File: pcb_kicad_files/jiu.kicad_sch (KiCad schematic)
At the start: 175 parts, among them J1 2x3 2.54mm pitch pin header, J2 TYPE-C-31-M-12, J3 1x5 2.54mm pitch pin header, J4 2x9 2.54mm pitch pin header, J5 RESET PINS, Q1 2N7002, SW1 1U, SW10 1U, SW11 1U, SW12 1U, SW13 1U, SW14 1U, SW15 1U, SW16 2u, SW17 1.5U, SW18 1U, SW19 1U, SW2 1U, SW20 1U, SW21 1U, SW22 1U, SW23 1U, SW24 1U, SW25 1U, SW26 1U, SW27 1U, SW28 1U, SW29 1U, SW3 1U, SW30 1.5U, SW31 1U, SW32 1.75U, SW33 1U, SW34 1U, SW35 1U, SW36 1U, SW37 1U, SW38 1U, SW39 1U, SW4 1U, SW40 1U, SW41 1U, SW42 1U, SW43 1U, SW44 2.25U, SW45 1U, SW46 1.25U, SW47 2.25U, SW48 1U, SW49 1U, SW5 1U, SW50 1U, SW51 1U, SW52 1U, SW53 1U, SW54 1U, SW55 1U, SW56 1U, SW57 1U, SW58 1.75U, SW59 1U, SW6 1U, SW60 1U, SW61 1.5U, SW62 1U, SW63 1.5U, SW64 7U, SW65 1.5U, SW66 1U, SW67 1U, SW68 1U, SW69 1.25U, SW7 1U, SW70 1.25U, SW71 1.25U, SW72 6.25U, SW73 1.25U, SW8 1U, SW9 1U, U1 SRV05-4-P-T7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

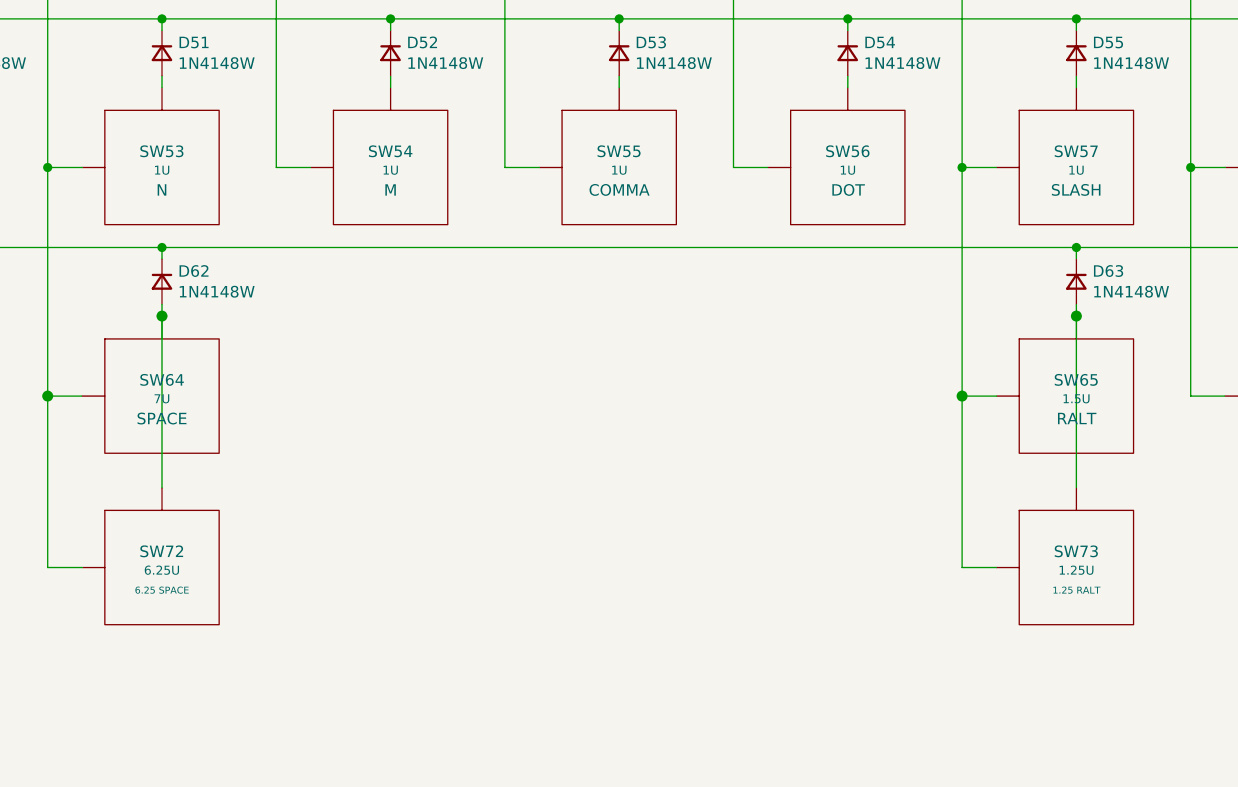
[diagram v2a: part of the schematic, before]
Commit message: Fix missing 6.25U bottom row key
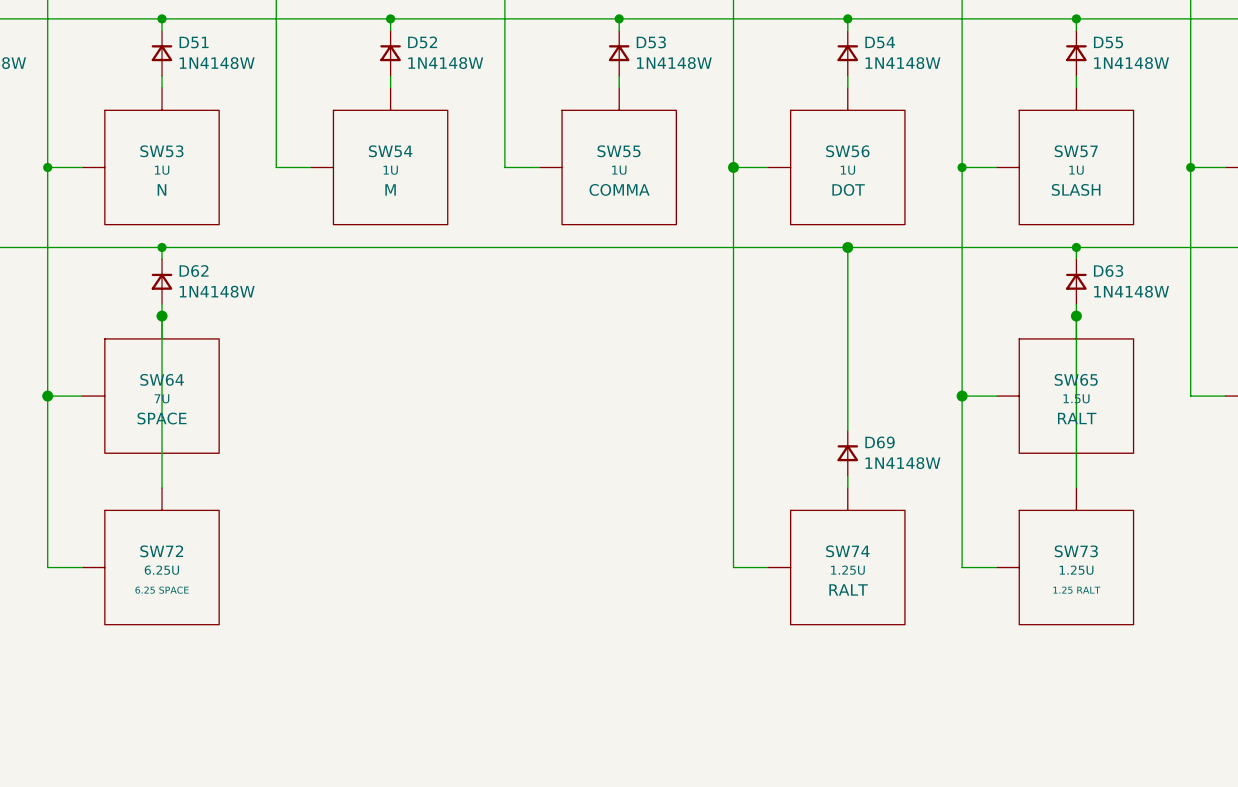
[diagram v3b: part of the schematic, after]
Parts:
- added D69: 1N4148W, acheron_Components:D_SOD-123, symbol Device:D_Small
- added SW74: 1.25U, acheron_MX_SolderMask:MX125, symbol acheronSymbols:MXSwitch
- D68: Manufacturer Shikues -> (none)
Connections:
- net C9: now also SW74.1 (Col)
- net R4: now also D69.1 (K)
- new net: D69.2 (A), SW74.2 (Row)
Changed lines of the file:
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@@
   (title_block
     (title "Jiu schematic")
-    (date "2021-02-21")
-    (rev "v1.1.8")
+    (date "2021-03-08")
+    (rev "v1.1.9")
     (company "Designed by Gondolindrim")
   )
@@
   (junction (at 266.7 76.2) (diameter 1.016) (color 0 0 0 0))
   (junction (at 266.7 101.6) (diameter 1.016) (color 0 0 0 0))
+  (junction (at 266.7 127) (diameter 1.2192) (color 0 0 0 0))
   (junction (at 271.145 332.105) (diameter 1.016) (color 0 0 0 0))
   (junction (at 271.145 338.455) (diameter 1.016) (color 0 0 0 0))
@@
   (junction (at 279.4 85.09) (diameter 1.016) (color 0 0 0 0))
   (junction (at 279.4 110.49) (diameter 1.016) (color 0 0 0 0))
+  (junction (at 279.4 135.89) (diameter 1.2192) (color 0 0 0 0))
   (junction (at 282.575 277.495) (diameter 1.016) (color 0 0 0 0))
   (junction (at 288.925 277.495) (diameter 1.016) (color 0 0 0 0))
@@
     (stroke (width 0) (type solid) (color 0 0 0 0))
   )
-  (wire (pts (xy 203.2 135.89) (xy 304.8 135.89))
+  (wire (pts (xy 203.2 135.89) (xy 279.4 135.89))
     (stroke (width 0) (type solid) (color 0 0 0 0))
   )
@@
     (stroke (width 0) (type solid) (color 0 0 0 0))
   )
+  (wire (pts (xy 266.7 127) (xy 266.7 171.45))
+    (stroke (width 0) (type solid) (color 0 0 0 0))
+  )
   (wire (pts (xy 270.51 76.2) (xy 266.7 76.2))
     (stroke (width 0) (type solid) (color 0 0 0 0))
@@
     (stroke (width 0) (type solid) (color 0 0 0 0))
   )
+  (wire (pts (xy 270.51 171.45) (xy 266.7 171.45))
+    (stroke (width 0) (type solid) (color 0 0 0 0))
+  )
   (wire (pts (xy 271.145 287.655) (xy 272.415 287.655))
     (stroke (width 0) (type solid) (color 0 0 0 0))
@@
     (stroke (width 0) (type solid) (color 0 0 0 0))
   )
+  (wire (pts (xy 279.4 135.89) (xy 279.4 156.21))
+    (stroke (width 0) (type solid) (color 0 0 0 0))
+  )
+  (wire (pts (xy 279.4 135.89) (xy 304.8 135.89))
+    (stroke (width 0) (type solid) (color 0 0 0 0))
+  )
+  (wire (pts (xy 279.4 161.29) (xy 279.4 162.56))
+    (stroke (width 0) (type solid) (color 0 0 0 0))
+  )
   (wire (pts (xy 282.575 273.05) (xy 282.575 277.495))
     (stroke (width 0) (type solid) (color 0 0 0 0))
@@
     (pin "2")
   )
+  (symbol (lib_id "Device:D_Small") (at 279.4 158.75 270) (unit 1)
+    (in_bom yes) (on_board yes)
+    (property "Reference" "D69" (id 0) (at 281.1781 157.6006 90)
+      (effects (font (size 1.27 1.27)) (justify left))
+    )
+    (property "Value" "1N4148W" (id 1) (at 281.1781 159.8993 90)
+      (effects (font (size 1.27 1.27)) (justify left))
+    )
+    (property "Footprint" "acheron_Components:D_SOD-123" (id 2) (at 279.4 158.75 90)
+      (effects (font (size 1.27 1.27)) hide)
+    )
+    (property "Datasheet" "~" (id 3) (at 279.4 158.75 90)
+      (effects (font (size 1.27 1.27)) hide)
+    )
+    (property "Package" "SOD-123" (id 4) (at 279.4 158.75 90)
+      (effects (font (size 1.27 1.27)) hide)
+    )
+    (pin "1")
+    (pin "2")
+  )
   (symbol (lib_id "Device:D_Small") (at 304.8 38.1 270) (unit 1)
     (in_bom yes) (on_board yes)
@@
       (effects (font (size 1.27 1.27)) hide)
     )
-    (property "Manufacturer" "Shikues" (id 4) (at 204.47 322.58 0)
-      (effects (font (size 1.27 1.27)) hide)
-    )
-    (property "LCSC Part Number" "C115330" (id 5) (at 204.47 322.58 0)
+    (property "LCSC Part Number" "C115330" (id 4) (at 204.47 322.58 0)
       (effects (font (size 1.27 1.27)) hide)
     )
@@
     (pin "2")
   )
+  (symbol (lib_id "acheronSymbols:MXSwitch") (at 279.4 171.45 0) (unit 1)
+    (in_bom no) (on_board yes)
+    (property "Reference" "SW74" (id 0) (at 279.4 169.6974 0))
+    (property "Value" "1.25U" (id 1) (at 279.4 171.7802 0)
+      (effects (font (size 0.9906 0.9906)))
+    )
+    (property "Footprint" "acheron_MX_SolderMask:MX125" (id 2) (at 279.4 171.45 0)
+      (effects (font (size 1.27 1.27)) hide)
+    )
+    (property "Datasheet" "" (id 3) (at 279.4 171.45 0)
+      (effects (font (size 1.27 1.27)) hide)
+    )
+    (property "Default keycode" "RALT" (id 4) (at 279.4 173.99 0))
+    (pin "1")
+    (pin "2")
+  )
   (symbol (lib_id "acheronSymbols:MXSwitch") (at 304.8 50.8 0) (unit 1)
     (in_bom no) (on_board yes)
@@
       (reference "D68") (unit 1) (value "RB060M-60") (footprint "acheron_Components:D_SOD-123")
     )
+    (path "/b11a079a-7715-44e5-8f45-742bb8e4c761"
+      (reference "D69") (unit 1) (value "1N4148W") (footprint "acheron_Components:D_SOD-123")
+    )
     (path "/0d47d058-12d7-4b9d-a82b-832091c19ada"
       (reference "F1") (unit 1) (value "mSMD110-16V") (footprint "acheron_Components:Fuse_1812_4532")
@@
       (reference "SW73") (unit 1) (value "1.25U") (footprint "acheron_MX_SolderMask:MX125")
     )
+    (path "/284362d5-314f-4ba3-9c4c-6f51d6510560"
+      (reference "SW74") (unit 1) (value "1.25U") (footprint "acheron_MX_SolderMask:MX125")
+    )
     (path "/c6a77dd8-927c-49d7-af6c-78d05d2184a0"

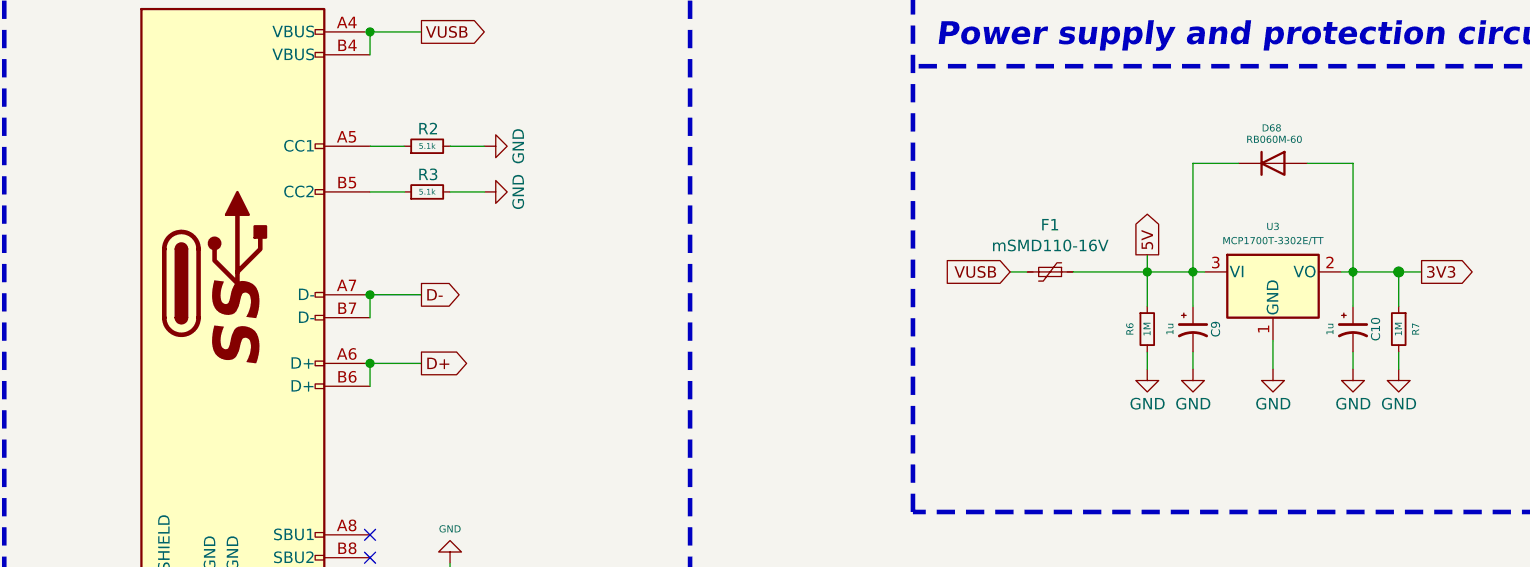
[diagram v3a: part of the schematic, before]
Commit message: gitignore, stab orientation
- Added backup files to gitignore
- Fix enter, right shift keys stab orientations
- New KiCAD version
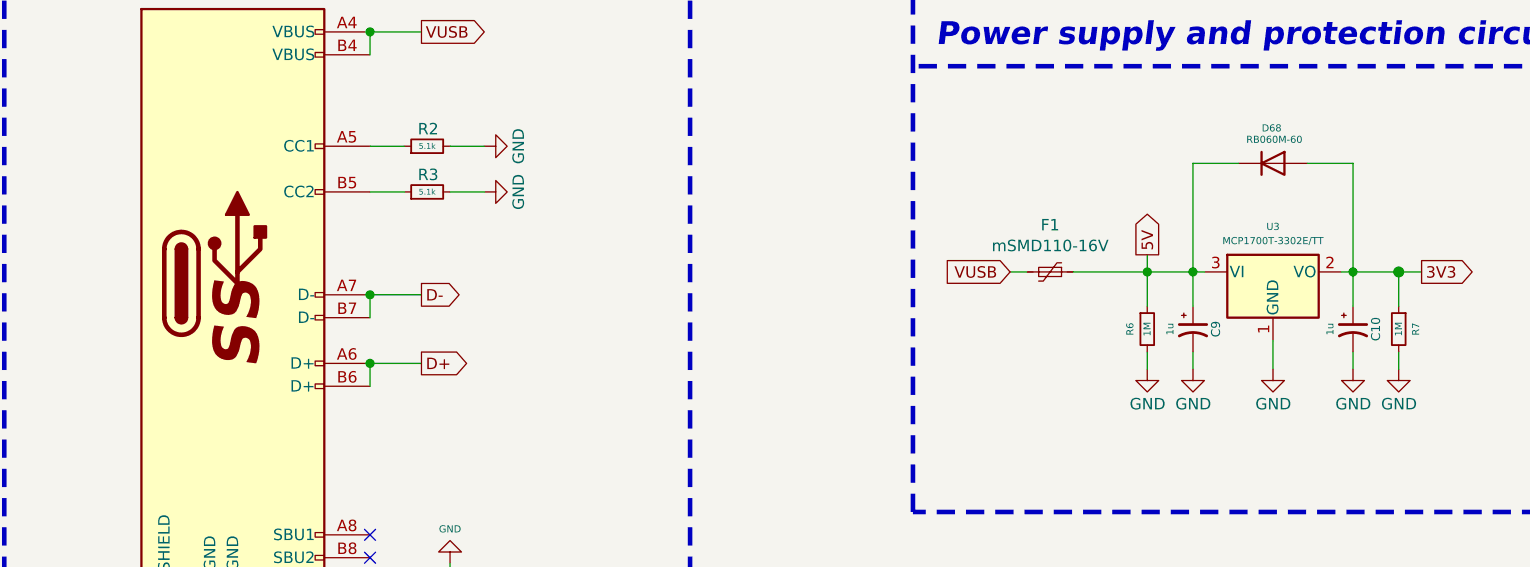
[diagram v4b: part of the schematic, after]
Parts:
- SW44: footprint acheron_MX_SolderMask:MX225R -> acheron_MX_SolderMask:MX225
- SW47: footprint acheron_MX_SolderMask:MX225 -> acheron_MX_SolderMask:MX225R

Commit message: Most MCU routing
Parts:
- removed C12: 4.7u, Capacitor_SMD:C_0402_1005Metric, symbol Device:C_Small
- removed C5: 100n, Capacitor_SMD:C_0402_1005Metric, symbol Device:C_Small
- removed J1: 2x3 2.54mm pitch pin header, acheron_Connectors:Conn_ARM_JTAG_SWD_6, symbol Connector_Generic:Conn_02x03_Odd_Even
- removed J3: 1x5 2.54mm pitch pin header, acheron_Connectors:PinHeader_1x5_P2.54mm_Vertical, symbol Connector_Generic:Conn_01x05
- removed J4: 2x9 2.54mm pitch pin header, acheron_Connectors:PinHeader_2x8_P2.54mm_Vertical, symbol Connector_Generic:Conn_02x08_Odd_Even
- removed U2: STM32F072CBT6, acheron_Components:LQFP-48_7x7mm_P0.5mm, symbol acheronSymbols:STM32F072-LQFP48
- added C1, C10, C4: 100n, Capacitor_SMD:C_0402_1005Metric, symbol Device:C_Small
- added C5: 10u, acheron_Components:CP_EIA-3216-10_Kemet-I_Pad1.58x1.35mm_HandSolder, symbol Device:CP1
- added C9: 16p, Capacitor_SMD:C_0402_1005Metric, symbol Device:C_Small
- added LED1, LED2: LED, acheron_Components:LED_THT_2.54mm, symbol acheronSymbols:LED
- added Q1, Q2: 2N7002, Package_TO_SOT_SMD:SOT-23, symbol Transistor_FET:2N7002
- added R1, R2, R4: 1.5k, Resistor_SMD:R_0402_1005Metric, symbol Device:R_Small
- added R11, R12, R3, R8: 10k, Resistor_SMD:R_0805_2012Metric, symbol Device:R_Small
- added R13: 100k, Resistor_SMD:R_0805_2012Metric, symbol Device:R_Small
- added R14, R7: 100, Resistor_SMD:R_0805_2012Metric, symbol Device:R_Small
- added R5: 0R, Resistor_SMD:R_0805_2012Metric, symbol Device:R_Small
- added R6: 1k, Resistor_SMD:R_0805_2012Metric, symbol Device:R_Small
- added SW75: K2-1187SQ-A4SW-06, acheron_Hardware:K2-1187SQ-A4SW-06, symbol Switch:SW_Push
- added U1: BL24C256A-SFRC, acheron_Components:TSSOP-8_4.4x3mm_P0.65mm, symbol Memory_EEPROM:24LC256
- added U2: STM32F411CEU6, acheron_Components:STM_UFQFPN-48_LQFP-48-1EP_7x7mm_P0.5mm_HandSoldering_ThermalReliefs, symbol acheron_Symbols:STM32F411-48
- added X1: ARM JTAG, acheron_Connectors:PinHeader_2x5_P2.54mm_Vertical_Staggered, symbol Connector_Generic:Conn_02x05_Odd_Even
- added Y1: 7325-0800A2010-00, acheron_Components:Crystal_SMD_3225-4Pin_3.2x2.5mm, symbol Device:Crystal_GND24
- C11: value 100n -> 4.7u; Specification MLCC 10V -> (none)
- C13: renamed from C1; value 4.7n -> 100n
- C14: renamed from C9; footprint acheron_Components:CP_EIA-3216-10_Kemet-I_Pad1.58x1.35mm_HandSolder -> Capacitor_SMD:C_0805_2012Metric; symbol Device:CP1_Small -> Device:C_Small; Package CT3216 -> C0805; Specification Tantallum 10V or more -> MLCC 10V or more
- C15: renamed from C10; footprint acheron_Components:CP_EIA-3216-10_Kemet-I_Pad1.58x1.35mm_HandSolder -> Capacitor_SMD:C_0805_2012Metric; symbol Device:CP1_Small -> Device:C_Small; Package CT3216 -> C0805; Specification Tantallum 10V or more -> MLCC 10V or more
- C2, C3: Specification MLCC 10V -> MLCC 10V or more
- C6: value 4.7u -> 1u; Specification MLCC 10V -> MLCC 10V or more
- C7: value 1u -> 10n; Specification MLCC 10V -> MLCC 10V or more
- C8: value 10n -> 16p; Specification MLCC 10V -> (none)
- R19: renamed from R6; value 1M -> 100k
- R20: renamed from R7; value 1M -> 100k
- renumbered C4 to C12, D69 to D67, D67 to D68, D68 to D69, J5 to J1, Q1 to Q3, R5 to R10, R1 to R15, R8 to R16, R3 to R17, R2 to R18, R4 to R9, SW74 to SW73, SW73 to SW74, U1 to U3, U3 to U4
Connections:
- net 3V3: now also C6.1, C1.2, C10.2, C4.2, C5.1, R1.1, R2.1, R4.1, SW75.1, U1.8 (VCC), U2.1 (VBAT), U2.24 (VDD), U2.36 (VDD), U2.48 (VDD), U2.9 (VDDA/VREF+), X1.7 (Pin_7), X1.8 (Pin_8); no longer C11.2, C6.2, C8.1
- net 5V: now also LED1.A, LED2.A, R5.1
- net BOOT0: now also R11.1, U2.44 (BOOT0), X1.6 (Pin_6)
- net C0: now also U2.12 (PA2)
- net C1: now also U2.11 (PA1)
- net C10: now also U2.45 (PB8)
- net C11: now also U2.4 (PC15_OSC32OUT)
- net C12: now also U2.46 (PB9)
- net C13: now also U2.3 (PC14_OSC32IN)
- net C14: now also U2.2 (PC13)
- net C2: now also U2.10 (PA0-WKUP)
- net C3: now also U2.19 (PB1)
- net C4: now also U2.21 (B10)
- net C5: now also U2.31 (PA10)
- net C6: now also U2.38 (PA15)
- net C7: now also U2.39 (PB3)
- net C8: now also U2.40 (PB4)
- net C9: now also U2.41 (PB5)
- net D+: now also R4.2, U2.33 (PA12)
- net D-: now also U2.32 (PA11)
- net GND: now also C6.2, C1.1, C10.1, C4.1, C5.2, C9.2, Q1.2 (S), Q2.2 (S), R13.2, R3.2, R8.1, U1.1 (A0), U1.2 (A1), U1.3 (A2), U1.4 (GND), U1.7 (WP), U2.23 (VSS), U2.35 (VSS), U2.47 (VSS), U2.8 (VSSA), X1.10 (Pin_10), X1.3 (Pin_3), X1.4 (Pin_4), Y1.2, Y1.4; no longer C6.1
- net NRST: now also U2.7 (NRST), X1.9 (Pin_9)
- net R0: now also U2.14 (PA4)
- net R1: now also U2.15 (PA5)
- net R2: now also U2.16 (PA6)
- net R3: now also U2.18 (PB0)
- net R4: now also U2.13 (PA3)
- net SWCLK: now also U2.37 (PA14), X1.2 (Pin_2)
- net SWDIO: now also U2.34 (PA13), X1.1 (Pin_1)
- net at R18.1: now also J2.B5 (CC2); no longer J2.A5 (CC1)
- net at R17.1: now also J2.A5 (CC1); no longer J2.B5 (CC2)
- net at Q3.1 (G), R16.2: now also R14.1; no longer D68.2 (A), J1.1 (Pin_1)
- net at Q3.3 (D), R15.1: now also R12.2
- new net: C11.2, U2.22 (VCAP_1)
- new net: Q2.1 (G), R12.1, R13.1
- new net: Q2.3 (D), R11.2
- new net: D68.2 (A), J1.1 (Pin_1), R14.2, SW75.2
- new net: Q1.1 (G), R7.1, R8.2
- new net: Q1.3 (D), R6.2
- new net: LED1.K, LED2.K, R6.1
- new net LED_PWM: R7.2, U2.17 (PA7)
- new net PA9: R5.2, U2.30 (PA9)
- new net PB2/BOOT1: R3.1, U2.20 (PB2), X1.5 (Pin_5)
- new net RGB_3V3: U2.28 (PB15)
- new net SCL: R2.2, U1.6 (SCL), U2.42 (PB6)
- new net SDA: R1.2, U1.5 (SDA), U2.43 (PB7)
- new net XTAL_IN: C9.1, U2.5 (PH0_OSCIN), Y1.3
- new net XTAL_OUT: C8.1, U2.6 (PH1_OSCOUT), Y1.1
- no-connect marks 2 -> 3
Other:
- note added: "(*) "Spooky pins": on STM32F4x1, pins A9 and B2 cannot be used for switch matrix: - A9 is meant to be used as a VBUS sensing. It has a undocumented internal pulldown resistor; - B2 is used as BOOT1 during bootup, so it needs an external pulldown for successful bootup"
- note added: "(**) PA9 jumper: a solderable jumper used to tie PA9 to VBUS. It is disconnected by default, hence PA9 is left floating"
- note added: "EEPROM"
- note added: "Spooky pin (*)"
- moved on the sheet: C12, C13, D1, D10, D11, D12, D13, D14, D15, D16, D17, D18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
